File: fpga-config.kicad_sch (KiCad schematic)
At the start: 21 parts, among them J1 PinHeader_2x7_P2mm_SMD_Shroud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, Q1 BSS138PW, Q2 BSS138PW, Q3 BSS138PW, SW1 CVS-03B, SW2 SW_KMR211NGLFS_SMD, U2 TPD4E05U06QDQARQ1, U4 XC7K160T-FFG676

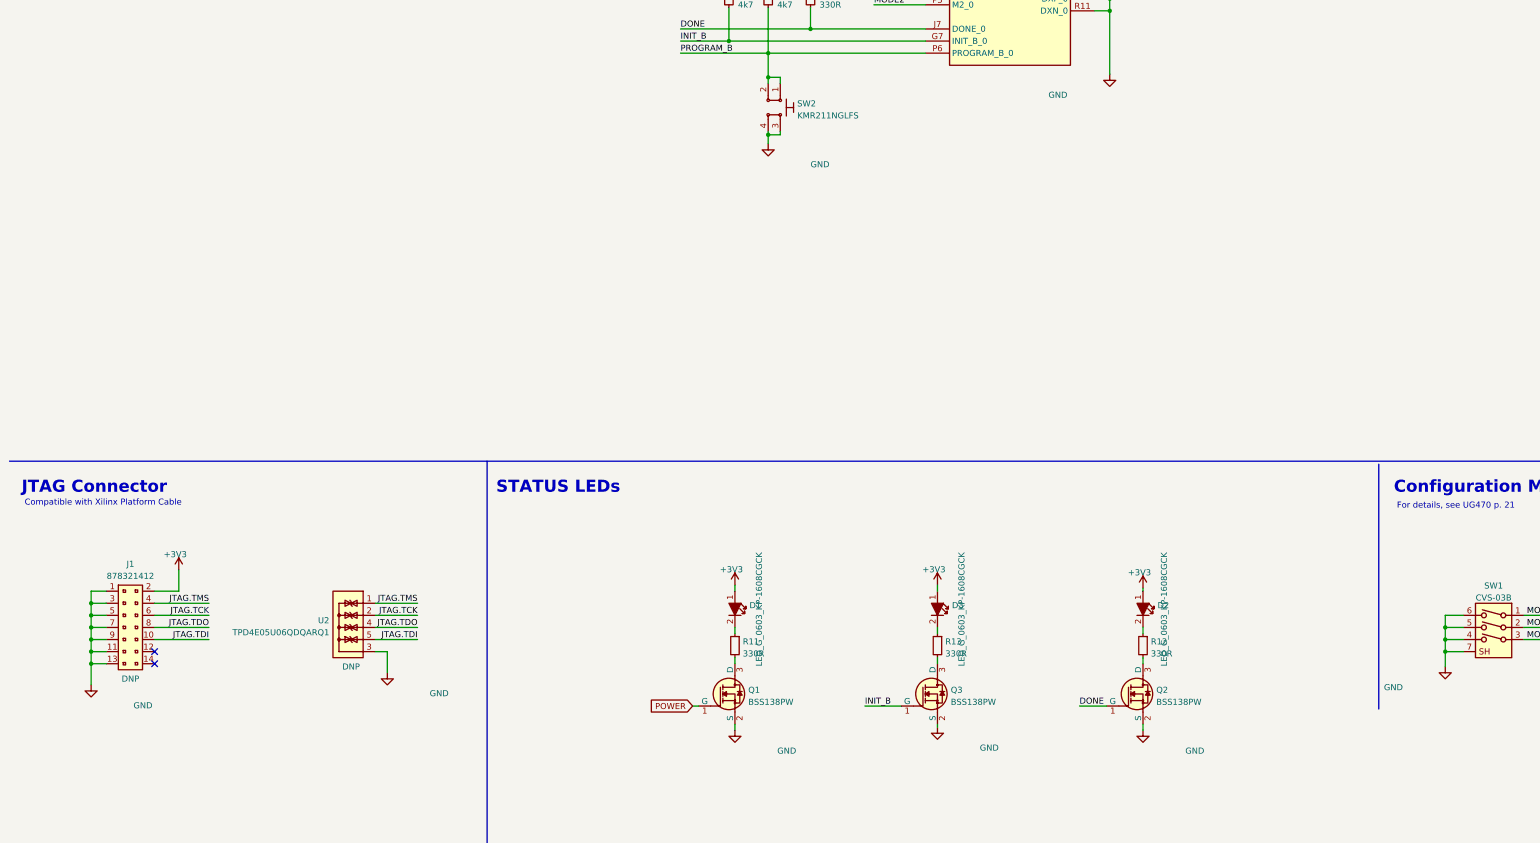
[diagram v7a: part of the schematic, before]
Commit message: Add updated components to local library
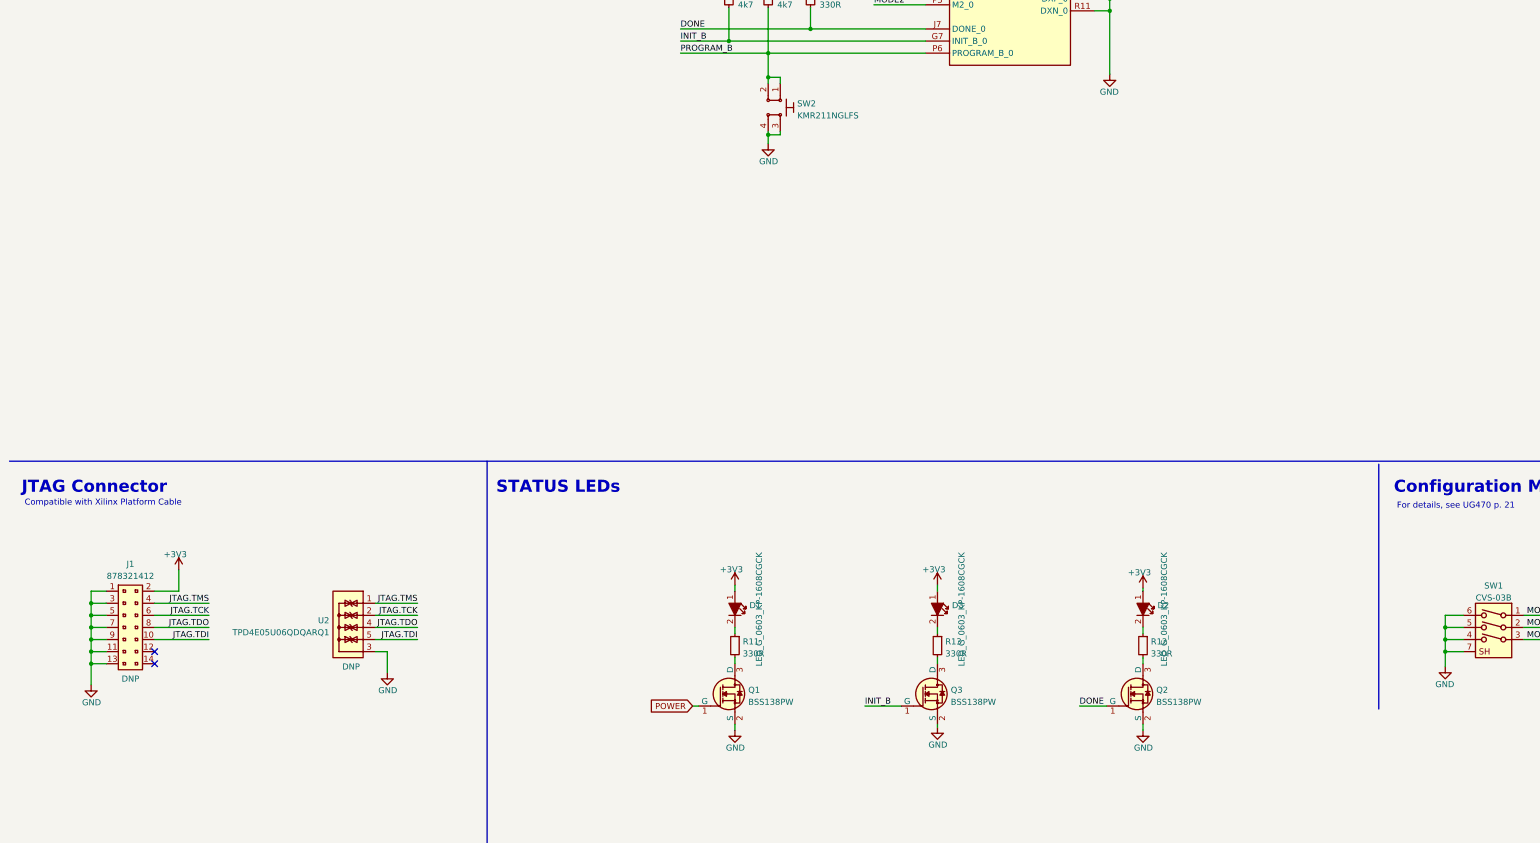
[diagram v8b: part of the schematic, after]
